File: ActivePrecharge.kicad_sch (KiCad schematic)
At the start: 52 parts, among them Con1 LED, IC1 1769205241, J1 Conn_01x03, J2 Conn_01x02, J3 Conn_01x02, Q1 IRLML0030, Q2 PMV35EPER, Q3 IRLML0030, U3 TLV9301xDCK, U4 TCMT1106

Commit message: finished for review
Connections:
- net HVGND: now also R7.1; no longer R7.2
- net Vref: now reaches C1.1, R1.2, R2.1, Ref_TP1.1, U3.1 (+)
- net Vref: now also R5.2; no longer R5.1
- net at Q1.2 (S), SigHV_TP1.1, U3.4: now also R5.1; no longer R5.2
- net at Q1.1 (G), R6.2: now also R7.2; no longer R7.1
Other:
- moved on the sheet: C1, C2, IN_TP1, Q1, R1, R2, R3, R4, R5, Ref_TP1, SigHV_TP1, U3

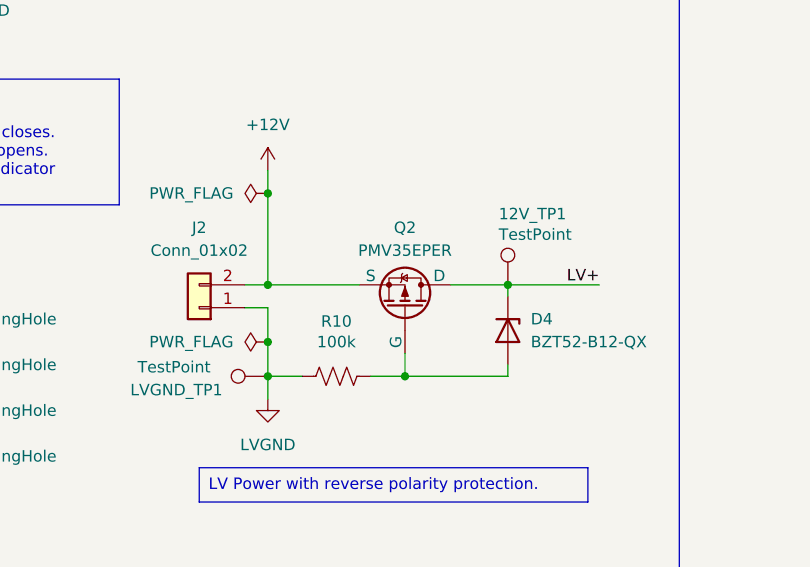
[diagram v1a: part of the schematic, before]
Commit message: fixed incorrect pmos pinout
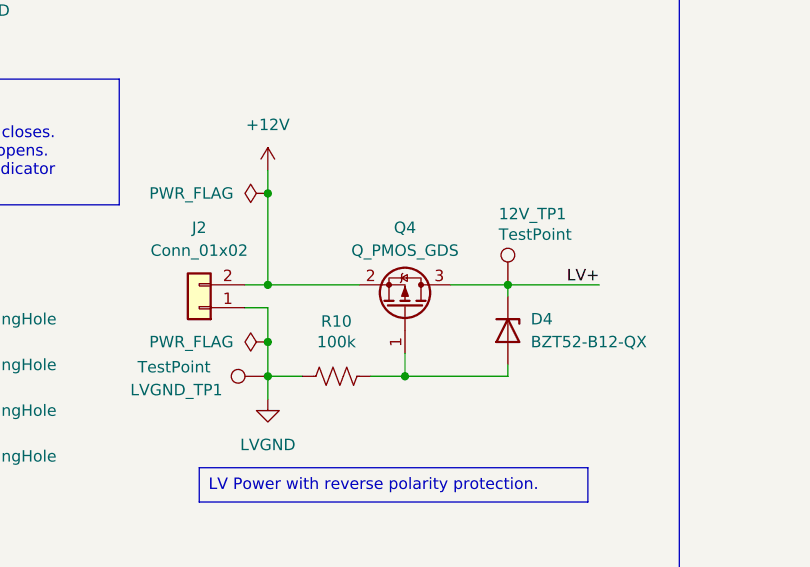
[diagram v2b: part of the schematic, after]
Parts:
- removed Q2: PMV35EPER, Package_TO_SOT_SMD:SOT-23-3, symbol Simulation_SPICE:PMOS
- added Q4: Q_PMOS_GDS, Package_TO_SOT_SMD:SOT-23-3, symbol Device:Q_PMOS_GDS
- 12V_TP1, Con-_TP1, HVG_TP1, HVI_TP1, HVR_TP1, IN_TP1, ISO_PWR_TP1, LVGND_TP1, OptVf_TP1, Ref_TP1, SigHV_TP1, SigLV_TP1: footprint Active-PrechargeLib:TestPoint_HEX_3mmID -> utsvt-special:TestPoint_HEX_3mmID
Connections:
- net +12V: now also Q4.2 (D)
- net LV+: now also Q4.3 (S)
- net at D4.2 (A), R10.2: now also Q4.1 (G)
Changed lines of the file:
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@@
 	)
 	(symbol
-		(lib_id "Simulation_SPICE:PMOS")
-		(at 250.19 109.22 270)
-		(mirror x)
-		(unit 1)
-		(exclude_from_sim no)
-		(in_bom yes)
-		(on_board yes)
-		(dnp no)
-		(property "Reference" "Q2"
-			(at 250.19 100.33 90)
-			(effects
-				(font
-					(size 1.27 1.27)
-				)
-			)
-		)
-		(property "Value" "PMV35EPER"
-			(at 250.19 102.87 90)
-			(effects
-				(font
-					(size 1.27 1.27)
-				)
-			)
-		)
-		(property "Footprint" "Package_TO_SOT_SMD:SOT-23-3"
-			(at 252.73 104.14 0)
-			(effects
-				(font
-					(size 1.27 1.27)
-				)
-				(hide yes)
-			)
-		)
-		(property "Datasheet" "https://ngspice.sourceforge.io/docs/ngspice-html-manual/manual.xhtml#cha_MOSFETs"
-			(at 237.49 109.22 0)
-			(effects
-				(font
-					(size 1.27 1.27)
-				)
-				(hide yes)
-			)
-		)
-		(property "Description" "P-MOSFET transistor, drain/source/gate"
-			(at 250.19 109.22 0)
-			(effects
-				(font
-					(size 1.27 1.27)
-				)
-				(hide yes)
-			)
-		)
-		(property "Sim.Device" "PMOS"
-			(at 233.045 109.22 0)
-			(effects
-				(font
-					(size 1.27 1.27)
-				)
-				(hide yes)
-			)
-		)
-		(property "Sim.Type" "VDMOS"
-			(at 231.14 109.22 0)
-			(effects
-				(font
-					(size 1.27 1.27)
-				)
-				(hide yes)
-			)
-		)
-		(property "Sim.Pins" "1=D 2=G 3=S"
-			(at 234.95 109.22 0)
-			(effects
-				(font
-					(size 1.27 1.27)
-				)
-				(hide yes)
-			)
-		)
-		(pin "3"
-		)
-		(pin "2"
-		)
-		(pin "1"
-		)
-		(instances
-			(project ""
-				(path "/b9847a31-2b3b-47ca-9561-fab506416f6d"
-					(reference "Q2")
-					(unit 1)
-				)
-			)
-		)
-	)
-	(symbol
 		(lib_id "power:+12V")
 		(at 261.62 40.64 0)
@@
 			)
 		)
-		(property "Footprint" "Active-PrechargeLib:TestPoint_HEX_3mmID"
+		(property "Footprint" "utsvt-special:TestPoint_HEX_3mmID"
 			(at 72.39 146.05 0)
 			(effects
@@
 	)
 	(symbol
+		(lib_id "Device:Q_PMOS_GDS")
+		(at 250.19 109.22 270)
+		(mirror x)
+		(unit 1)
+		(exclude_from_sim no)
+		(in_bom yes)
+		(on_board yes)
+		(dnp no)
+		(fields_autoplaced yes)
+		(property "Reference" "Q4"
+			(at 250.19 100.33 90)
+			(effects
+				(font
+					(size 1.27 1.27)
+				)
+			)
+		)
+		(property "Value" "Q_PMOS_GDS"
+			(at 250.19 102.87 90)
+			(effects
+				(font
+					(size 1.27 1.27)
+				)
+			)
+		)
+		(property "Footprint" "Package_TO_SOT_SMD:SOT-23-3"
+			(at 252.73 104.14 0)
+			(effects
+				(font
+					(size 1.27 1.27)
+				)
+				(hide yes)
+			)
+		)
+		(property "Datasheet" "~"
+			(at 250.19 109.22 0)
+			(effects
+				(font
+					(size 1.27 1.27)
+				)
+				(hide yes)
+			)
+		)
+		(property "Description" "P-MOSFET transistor, gate/drain/source"
+			(at 250.19 109.22 0)
+			(effects
+				(font
+					(size 1.27 1.27)
+				)
+				(hide yes)
+			)
+		)
+		(pin "3"
+		)
+		(pin "1"
+		)
+		(pin "2"
+		)
+		(instances
+			(project ""
+				(path "/b9847a31-2b3b-47ca-9561-fab506416f6d"
+					(reference "Q4")
+					(unit 1)
+				)
+			)
+		)
+	)
+	(symbol
 		(lib_id "Connector:TestPoint")
 		(at 180.34 59.69 0)
@@
 			)
 		)
-		(property "Footprint" "Active-PrechargeLib:TestPoint_HEX_3mmID"
+		(property "Footprint" "utsvt-special:TestPoint_HEX_3mmID"
 			(at 185.42 59.69 0)
 			(effects
@@
 			)
 		)
-		(property "Footprint" "Active-PrechargeLib:TestPoint_HEX_3mmID"
+		(property "Footprint" "utsvt-special:TestPoint_HEX_3mmID"
 			(at 50.8 29.21 0)
 			(effects
@@
 			)
 		)
-		(property "Footprint" "Active-PrechargeLib:TestPoint_HEX_3mmID"
+		(property "Footprint" "utsvt-special:TestPoint_HEX_3mmID"
 			(at 50.8 54.61 0)
 			(effects
@@
 			)
 		)
-		(property "Footprint" "Active-PrechargeLib:TestPoint_HEX_3mmID"
+		(property "Footprint" "utsvt-special:TestPoint_HEX_3mmID"
 			(at 234.95 111.76 0)
 			(effects
@@
 			)
 		)
-		(property "Footprint" "Active-PrechargeLib:TestPoint_HEX_3mmID"
+		(property "Footprint" "utsvt-special:TestPoint_HEX_3mmID"
 			(at 140.97 92.71 0)
 			(effects
@@
 			)
 		)
-		(property "Footprint" "Active-PrechargeLib:TestPoint_HEX_3mmID"
+		(property "Footprint" "utsvt-special:TestPoint_HEX_3mmID"
 			(at 203.2 54.61 0)
 			(effects
@@
 			)
 		)
-		(property "Footprint" "Active-PrechargeLib:TestPoint_HEX_3mmID"
+		(property "Footprint" "utsvt-special:TestPoint_HEX_3mmID"
 			(at 129.54 41.91 0)
 			(effects
@@
 			)
 		)
-		(property "Footprint" "Active-PrechargeLib:TestPoint_HEX_3mmID"
+		(property "Footprint" "utsvt-special:TestPoint_HEX_3mmID"
 			(at 266.7 106.68 0)
 			(effects
@@
 			)
 		)
-		(property "Footprint" "Active-PrechargeLib:TestPoint_HEX_3mmID"
+		(property "Footprint" "utsvt-special:TestPoint_HEX_3mmID"
 			(at 82.55 39.37 0)
 			(effects
@@
 			)
 		)
-		(property "Footprint" "Active-PrechargeLib:TestPoint_HEX_3mmID"
+		(property "Footprint" "utsvt-special:TestPoint_HEX_3mmID"
 			(at 64.77 152.4 0)
 			(effects
@@
 			)
 		)
-		(property "Footprint" "Active-PrechargeLib:TestPoint_HEX_3mmID"
+		(property "Footprint" "utsvt-special:TestPoint_HEX_3mmID"
 			(at 99.06 149.86 0)
 			(effects

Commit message: pretty sch changxu approved
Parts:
- added C5: 0.1u, Capacitor_SMD:C_0805_2012Metric, symbol Device:C
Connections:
- net HVGND: now also C5.2
- net ISO_PWR: now also R8.2, C5.1; no longer R8.1
- net at OptVf_TP1.1, U4.1: now also R8.1; no longer R8.2
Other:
- removed sheet Untitled Sheet
- note added: "(except optocoupler and isolated DCDC converter which bridges HV and LV)"
- note added: "(except optocoupler and isolated DCDC convertor which bridges HV and LV)"
- note added: "Contactor Indicator LED"
- note added: "Flyback Diode"
- note added: "HV Circuitry"
- note added: "LV Circuitry"
- note added: "Optocoupler (Galvonic isolation)"
- note removed: "HV Circuitry (except optocoupler and isolated DCDC converter which bridges HV and LV)"
- note removed: "LV Circuitry (except optocoupler and isolated DCDC convertor which bridges HV and LV)"
- moved on the sheet: 12V_TP1, C1, C2, C3, C4, Con-_TP1, Con1, D1, D2, D3, D4, D5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

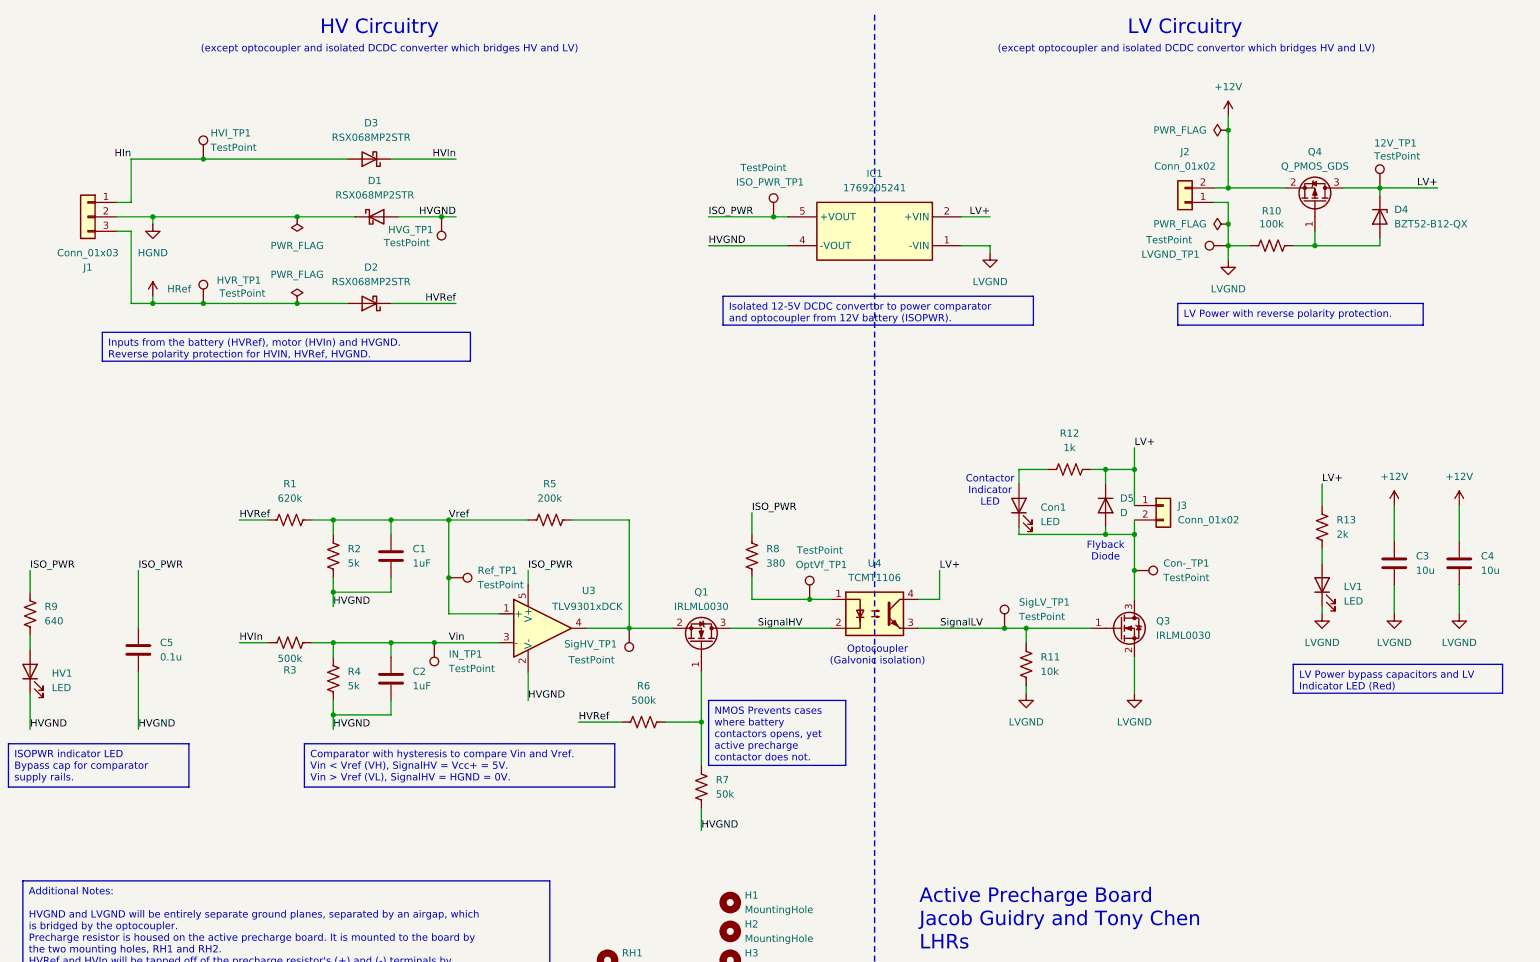
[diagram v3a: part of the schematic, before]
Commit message: started hv layout rework w/ fuses, changed lv layout connectors
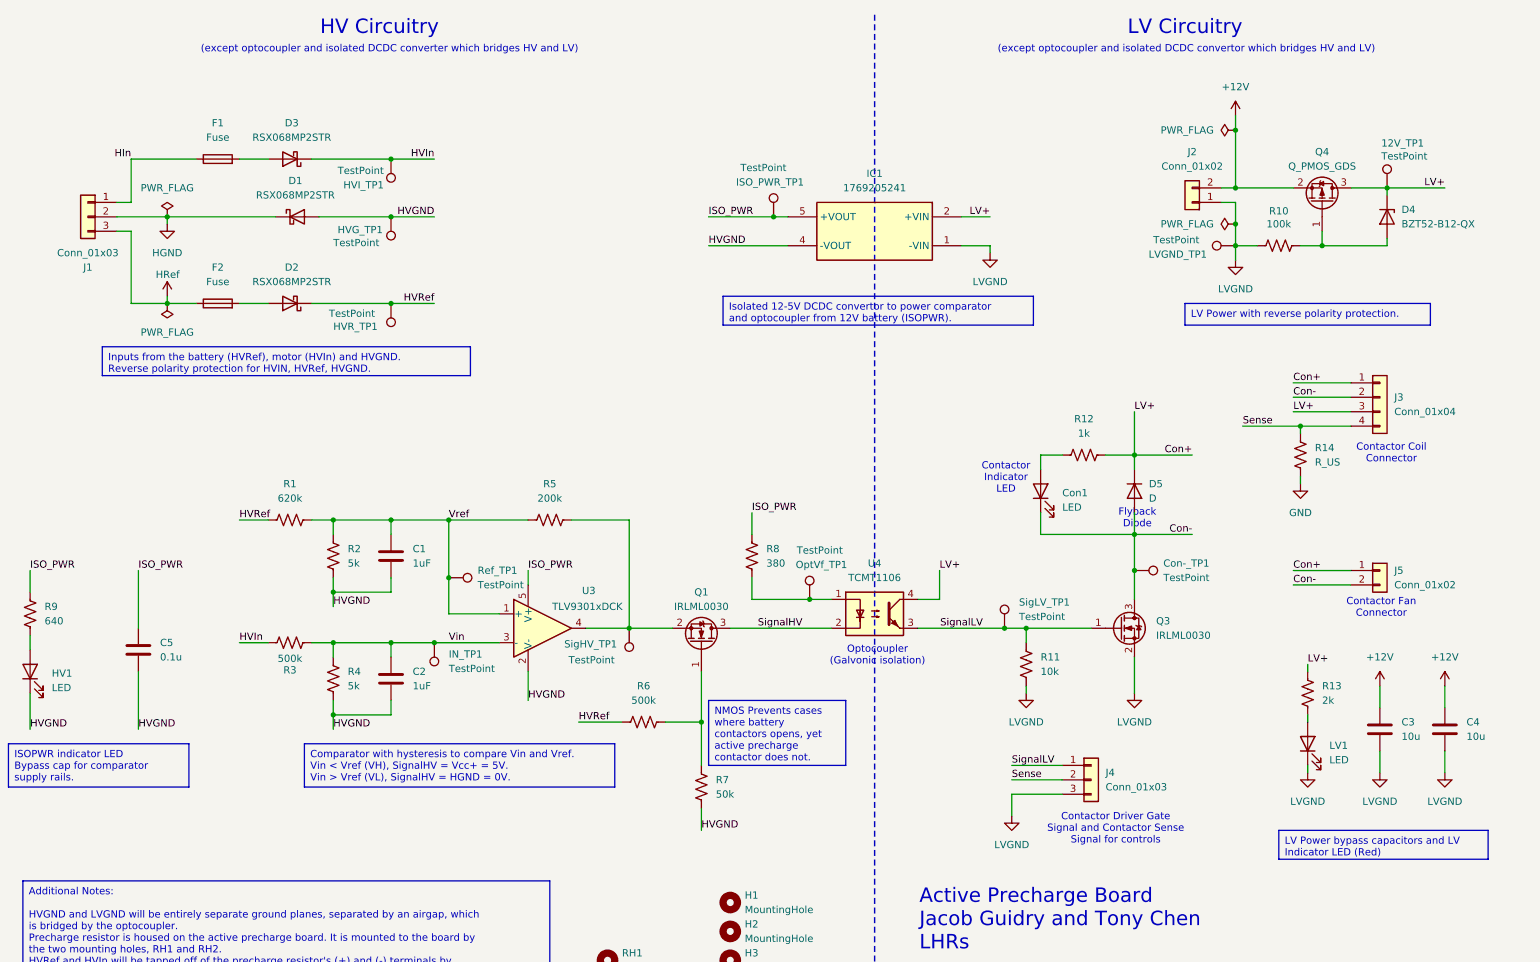
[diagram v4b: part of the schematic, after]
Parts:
- removed J3: Conn_01x02, utsvt-conn:Molex_MicroFit3.0_1x2xP3.00mm_PolarizingPeg_Vertical, symbol Connector_Generic:Conn_01x02
- added F1, F2: Fuse, Fuse:Fuseholder_Blade_Mini_Keystone_3568, symbol Device:Fuse
- added J3: Conn_01x04, utsvt-conn:Molex_MicroFit3.0_1x4xP3.00mm_PolarizingPeg_Vertical, symbol Connector_Generic:Conn_01x04
- added J4: Conn_01x03, utsvt-conn:Molex_MicroFit3.0_1x3xP3.00mm_PolarizingPeg_Vertical, symbol Connector_Generic:Conn_01x03
- added J5: Conn_01x02, utsvt-conn:Molex_MicroFit3.0_1x2xP3.00mm_PolarizingPeg_Vertical, symbol Connector_Generic:Conn_01x02
- added R14: R_US, symbol Device:R_US
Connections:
- net HIn: now also F1.1; no longer D3.2 (A), HVI_TP1.1
- net HRef: now also F2.1; no longer D2.2 (A), HVR_TP1.1
- net HVIn: now also HVI_TP1.1
- net HVRef: now also HVR_TP1.1
- net LVGND: now also J4.3 (Pin_3)
- net SignalLV: now also J4.1 (Pin_1)
- net Con-: now reaches Con-_TP1.1, Con1.1 (K), D5.2 (A), Q3.3 (D)
- net Con-: now also J3.2 (Pin_2), J5.2 (Pin_2)
- net LV+ renamed Con+
- net Con+: now also J3.1 (Pin_1), J3.3 (Pin_3), J5.1 (Pin_1)
- new net: D2.2 (A), F2.2
- new net: D3.2 (A), F1.2
- new net GND: R14.1
- new net Sense: J3.4 (Pin_4), J4.2 (Pin_2), R14.2
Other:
- note added: "Contactor Coil Connector"
- note added: "Contactor Driver Gate Signal and Contactor Sense Signal for controls"
- note added: "Contactor Fan Connector"
- moved on the sheet: 12V_TP1, C3, C4, Con1, D1, D2, D3, D4, D5, HVG_TP1, HVI_TP1, HVR_TP1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

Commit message: all layout and sch changes finished, ready for frank to review
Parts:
- removed Con-_TP1, HVI_TP1, HVR_TP1: TestPoint, utsvt-special:TestPoint_HEX_3mmID, symbol Connector:TestPoint
- removed H3, H4: MountingHole, MountingHole:MountingHole_3mm, symbol Mechanical:MountingHole
- removed J3: Conn_01x04, utsvt-conn:Molex_MicroFit3.0_1x4xP3.00mm_PolarizingPeg_Vertical, symbol Connector_Generic:Conn_01x04
- removed J5: Conn_01x02, utsvt-conn:Molex_MicroFit3.0_1x2xP3.00mm_PolarizingPeg_Vertical, symbol Connector_Generic:Conn_01x02
- removed R14: R_US, symbol Device:R_US
- added J3: Conn_02x03_Top_Bottom, Active-PrechargeLib:CONN_SD-43045-005_06_MOL, symbol Connector_Generic:Conn_02x03_Top_Bottom
- added R15: 10k, Resistor_SMD:R_0805_2012Metric, symbol Device:R_US
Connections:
- net Con+: now also J3.1 (Pin_1), J3.4 (Pin_4), J3.5 (Pin_5)
- net Con-: now also J3.3 (Pin_3), J3.6 (Pin_6)
- net LVGND: now also J4.2 (Pin_2), R15.1; no longer J4.3 (Pin_3)
- net Sense: now also J4.1 (Pin_1), J3.2 (Pin_2), R15.2; no longer J4.2 (Pin_2)
- net SignalLV: now also J4.3 (Pin_3); no longer J4.1 (Pin_1)
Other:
- note added: "Coil+"
- note added: "Coil-"
- note added: "Fan+"
- note added: "Fan-"
- note removed: "Contactor Coil Connector"
- note removed: "Contactor Fan Connector"
- moved on the sheet: D1, H1, H2, HVG_TP1, SigLV_TP1

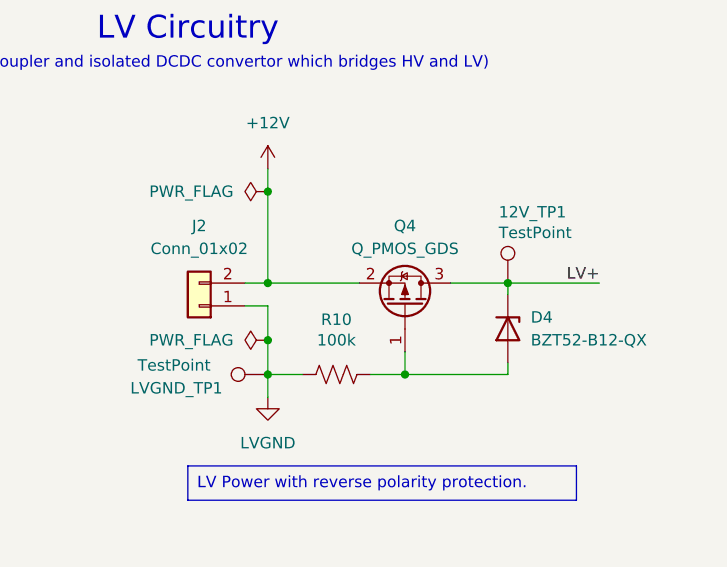
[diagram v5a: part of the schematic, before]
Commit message: v.3 ordered, fixed lv reverse polarity pmos body diode
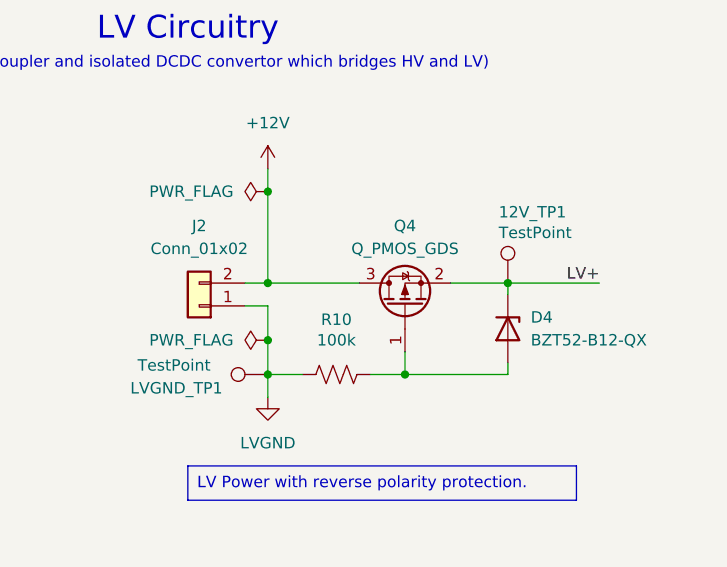
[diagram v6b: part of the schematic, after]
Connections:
- net +12V: now also Q4.3 (S); no longer Q4.2 (D)
- net Con+: now also Q4.2 (D); no longer Q4.3 (S)
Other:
- moved on the sheet: Q4
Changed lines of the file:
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@@
 	(symbol
 		(lib_id "Device:Q_PMOS_GDS")
-		(at 248.92 46.99 270)
-		(mirror x)
+		(at 248.92 46.99 90)
 		(unit 1)
 		(exclude_from_sim no)
@@
 		(on_board yes)
 		(dnp no)
-		(fields_autoplaced yes)
 		(property "Reference" "Q4"
 			(at 248.92 38.1 90)
@@
 		)
 		(property "Footprint" "Package_TO_SOT_SMD:SOT-23-3"
-			(at 251.46 41.91 0)
+			(at 246.38 41.91 0)
 			(effects
 				(font

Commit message: friday meeting for tony
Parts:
- R9: value 640 -> 750
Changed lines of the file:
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@@
 			)
 		)
-		(property "Value" "640"
+		(property "Value" "750"
 			(at 24.13 120.6499 0)
 			(effects
